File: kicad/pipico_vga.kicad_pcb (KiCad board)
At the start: 2 copper layers, 47 parts, among them J1 Conn_01x15, J2 DB15_Male_HighDensity_Mountin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, U1 Pico, U2 74LVC162244ADGVJ

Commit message: progress on pcb rev2
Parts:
- moved TP4 99.9 mm to (160.4, 106.9)
- moved R22 94.0 mm to (115.9, 94.5), turned to 180 degrees
- moved R17 94.0 mm to (116.8, 97.1), turned to 270 degrees
- moved R21 92.6 mm to (114.1, 92.8), turned to 180 degrees
- moved R16 91.6 mm to (115.0, 97.1), turned to 270 degrees
- moved R20 89.3 mm to (112.4, 94.5), turned to 180 degrees
- moved R15 89.2 mm to (113.2, 97.1), turned to 270 degrees
- moved TP6 89.1 mm to (156.2, 115.7), turned to 180 degrees
- moved U1 88.5 mm to (114.2, 109.1)
- moved R19 88.1 mm to (110.6, 92.8), turned to 180 degrees
- moved R14 86.8 mm to (111.5, 97.1), turned to 270 degrees
- moved R18 84.7 mm to (108.9, 94.5), turned to 180 degrees
- moved R13 84.5 mm to (109.8, 97.1), turned to 270 degrees
- moved C1 84.3 mm to (111.8, 102.2), turned to 90 degrees
- moved C4 83.4 mm to (113.8, 102.2), turned to 90 degrees
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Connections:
- net Net-(R15-Pad2) renamed /r2
- J1 pad 11: Net-(J1-Pad11) -> +3V3
- J1 pad 5: +3V3 -> Net-(J1-Pad5)
- R13 pad 2: Net-(R13-Pad2) -> /r0
- R14 pad 2: Net-(R14-Pad2) -> /r1
- R16 pad 2: Net-(R16-Pad2) -> /r3
- R17 pad 2: Net-(R17-Pad2) -> /r4
- R2 pad 2: Net-(R2-Pad2) -> /g0
- R24 pad 2: Net-(R24-Pad2) -> /b0
- R25 pad 2: Net-(R25-Pad2) -> /b1
- R26 pad 2: Net-(R26-Pad2) -> /b2
- R27 pad 2: Net-(R27-Pad2) -> /b3
- R28 pad 2: Net-(R28-Pad2) -> /b4
- R3 pad 2: Net-(R3-Pad2) -> /g1
- R4 pad 2: Net-(R4-Pad2) -> /g2
- R5 pad 2: Net-(R5-Pad2) -> /g3
- R6 pad 2: Net-(R6-Pad2) -> /g4
- U1 pad 21: /vga_data -> /hsync
- U1 pad 22: /vga_clk -> /vsync
- U1 pad 24: /vsync -> /vga_data
- U1 pad 25: /hsync -> /vga_clk
- U1 pad 26: Net-(J1-Pad15) -> Net-(J1-Pad1)
- U1 pad 27: Net-(J1-Pad14) -> Net-(J1-Pad2)
- U1 pad 29: Net-(J1-Pad12) -> Net-(J1-Pad4)
- U1 pad 30: Net-(J1-Pad11) -> Net-(J1-Pad5)
- U1 pad 31: Net-(J1-Pad10) -> Net-(J1-Pad6)
- U1 pad 32: Net-(J1-Pad9) -> Net-(J1-Pad7)
- U1 pad 34: Net-(J1-Pad7) -> Net-(J1-Pad9)
- U1 pad 35: Net-(J1-Pad6) -> Net-(J1-Pad10)
- U1 pad 37: Net-(J1-Pad4) -> Net-(J1-Pad12)
- U1 pad 39: Net-(J1-Pad2) -> Net-(J1-Pad14)
- U1 pad 40: Net-(J1-Pad1) -> Net-(J1-Pad15)
- U2 pad 11: /gpio6 -> /gpio8
- U2 pad 13: /gpio8 -> /gpio6
- U2 pad 14: /gpio9 -> /gpio5
- U2 pad 16: /gpio10 -> /gpio4
- U2 pad 17: /gpio11 -> /gpio3
- U2 pad 19: /gpio12 -> /gpio2
- U2 pad 2: /gpio0 -> /gpio14
- U2 pad 20: /gpio13 -> /gpio1
- U2 pad 22: /gpio14 -> /gpio0
- U2 pad 27: Net-(R17-Pad2) -> /r0
- U2 pad 29: Net-(R16-Pad2) -> /r1
- U2 pad 3: /gpio1 -> /gpio13
- U2 pad 32: Net-(R14-Pad2) -> /r3
- U2 pad 33: Net-(R13-Pad2) -> /r4
- U2 pad 35: Net-(R6-Pad2) -> /b0
- U2 pad 36: Net-(R5-Pad2) -> /b1
- U2 pad 37: Net-(R4-Pad2) -> /b2
- U2 pad 38: Net-(R3-Pad2) -> /b3
- U2 pad 40: Net-(R2-Pad2) -> /b4
- U2 pad 41: Net-(R28-Pad2) -> /g0
- U2 pad 43: Net-(R27-Pad2) -> /g1
- U2 pad 44: Net-(R26-Pad2) -> /g2
- U2 pad 46: Net-(R25-Pad2) -> /g3
- U2 pad 47: Net-(R24-Pad2) -> /g4
- U2 pad 5: /gpio3 -> /gpio12
- U2 pad 6: (no net) -> /gpio11
- U2 pad 8: /gpio4 -> /gpio10
- U2 pad 9: /gpio5 -> /gpio9
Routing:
- net /vga_data: track 95.4 -> 0.00 mm
- net /hsync: track 79.4 -> 0.00 mm
- net /vsync: track 76.6 -> 0.00 mm
- net /vga_clk: track 75.5 -> 0.00 mm
- net +3V3: track 125.0 -> 72.8 mm, vias 5 -> 4
- net GND: track 71.3 -> 26.1 mm, vias 9 -> 0
- net /b0: track 0.00 -> 24.9 mm, vias 0 -> 2
- net /b1: track 0.00 -> 22.8 mm, vias 0 -> 2
- net /b2: track 0.00 -> 21.8 mm, vias 0 -> 2
- net /b3: track 0.00 -> 19.7 mm, vias 0 -> 2
- net /b4: track 0.00 -> 18.2 mm, vias 0 -> 2
- net /red: track 38.1 -> 55.8 mm, vias 0 -> 2
- net /gpio2: track 0.00 -> 14.0 mm
- net Net-(R17-Pad2): track 12.5 -> 0.00 mm
- net Net-(R16-Pad2): track 11.9 -> 0.00 mm
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- removed copper zone on B.Cu, net GND
- removed copper zone on F.Cu, net GND
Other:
- net class Default: clearance 0.2 -> 0.3; via_dia 1.5 -> 0.8
- net class tiny added: clearance 0.2, trace_width 0.3, via_dia 0.8, via_drill 0.4
- rule trace_clearance: 0.2 -> 0.3
- board text removed: "PICO VGA V2 Anton Lööf"

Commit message: Add v2 PCB
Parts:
- BLUE: renamed from TP3; footprint TestPoint:TestPoint_Pad_D1.5mm -> TestPoint:TestPoint_THTPad_D2.0mm_Drill1.0mm; moved to B.Cu
- C1, C2, C3, C4, J1, J2, U1: moved to F.Cu
- GND: renamed from TP6; footprint TestPoint:TestPoint_Pad_D1.5mm -> TestPoint:TestPoint_THTPad_D2.0mm_Drill1.0mm; moved to B.Cu
- GND: renamed from TP5; footprint TestPoint:TestPoint_Pad_D1.5mm -> TestPoint:TestPoint_THTPad_D2.0mm_Drill1.0mm; moved to B.Cu
- GND: renamed from TP4; footprint TestPoint:TestPoint_Pad_D1.5mm -> TestPoint:TestPoint_THTPad_D2.0mm_Drill1.0mm; moved to B.Cu
- GREEN: renamed from TP2; footprint TestPoint:TestPoint_Pad_D1.5mm -> TestPoint:TestPoint_THTPad_D2.0mm_Drill1.0mm; moved to B.Cu
- R1, R10, R11, R12, R13, R14, R15, R16, R17, R18, R19, R2, R20, R21, R22, R23, R24, R25, R26, R27, R28, R29, R3, R30, R31, R32, R33, R4, R5, R6, R7, R8, R9, U2: moved to B.Cu
- RED: renamed from TP1; footprint TestPoint:TestPoint_Pad_D1.5mm -> TestPoint:TestPoint_THTPad_D2.0mm_Drill1.0mm; moved to B.Cu
- moved J2 67.4 mm to (137.7, 79.4)
- moved RED 57.9 mm to (131.8, 85.0)
- moved BLUE 53.9 mm to (131.8, 93.0), turned to 270 degrees
- moved GREEN 52.4 mm to (131.8, 89.0)
- moved R30 51.2 mm to (146.9, 89.0)
- moved R32 51.2 mm to (143.4, 89.0)
- moved R29 48.5 mm to (148.6, 90.8)
- moved R31 48.5 mm to (145.1, 90.8)
- moved R33 48.5 mm to (141.6, 90.8)
- moved GND 46.5 mm to (126.8, 89.0)
- moved R19 45.6 mm to (142.6, 125.2)
- moved R21 45.6 mm to (146.1, 125.2)
- moved R23 44.7 mm to (149.5, 93.4), turned to 270 degrees
- moved R24 44.7 mm to (147.8, 93.4), turned to 270 degrees
- moved R25 44.7 mm to (146.0, 93.4), turned to 270 degrees
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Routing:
- net /vga_clk: track 0.00 -> 50.2 mm
- net GND: track 26.1 -> 74.2 mm, vias 0 -> 3
- net /vsync: track 0.00 -> 32.4 mm
- net /vga_data: track 0.00 -> 29.3 mm
- net /blue: track 13.4 -> 38.6 mm
- net +3V3: track 72.8 -> 49.2 mm
- net /hsync: track 0.00 -> 22.4 mm
- net /green: track 22.5 -> 35.2 mm
- net /red: track 55.8 -> 64.7 mm, vias 2 -> 1
- added copper zone on B.Cu, net GND
- added copper zone on F.Cu, net GND
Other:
- board outline added: 37 x 67 mm
- board text added: "Anton Lööf 2021 REV2"
- board text added: "Raspberry pi Pico VGA"
- board text added: "VBUS VSYS GND 3V3EN 3V3 AREF GP28 GND GP27 GP26 RUN GP22 GND GP21 GP20"

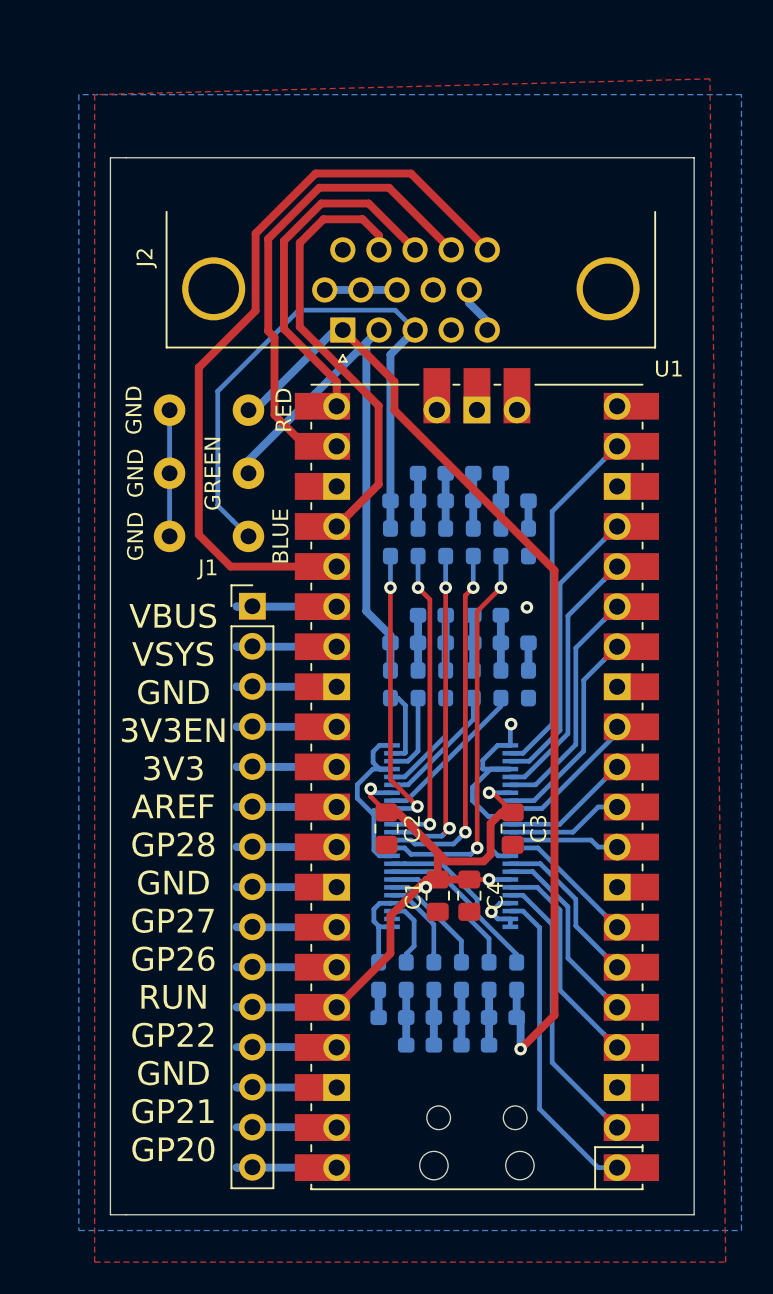
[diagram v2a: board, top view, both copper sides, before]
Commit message: Add mounting hole
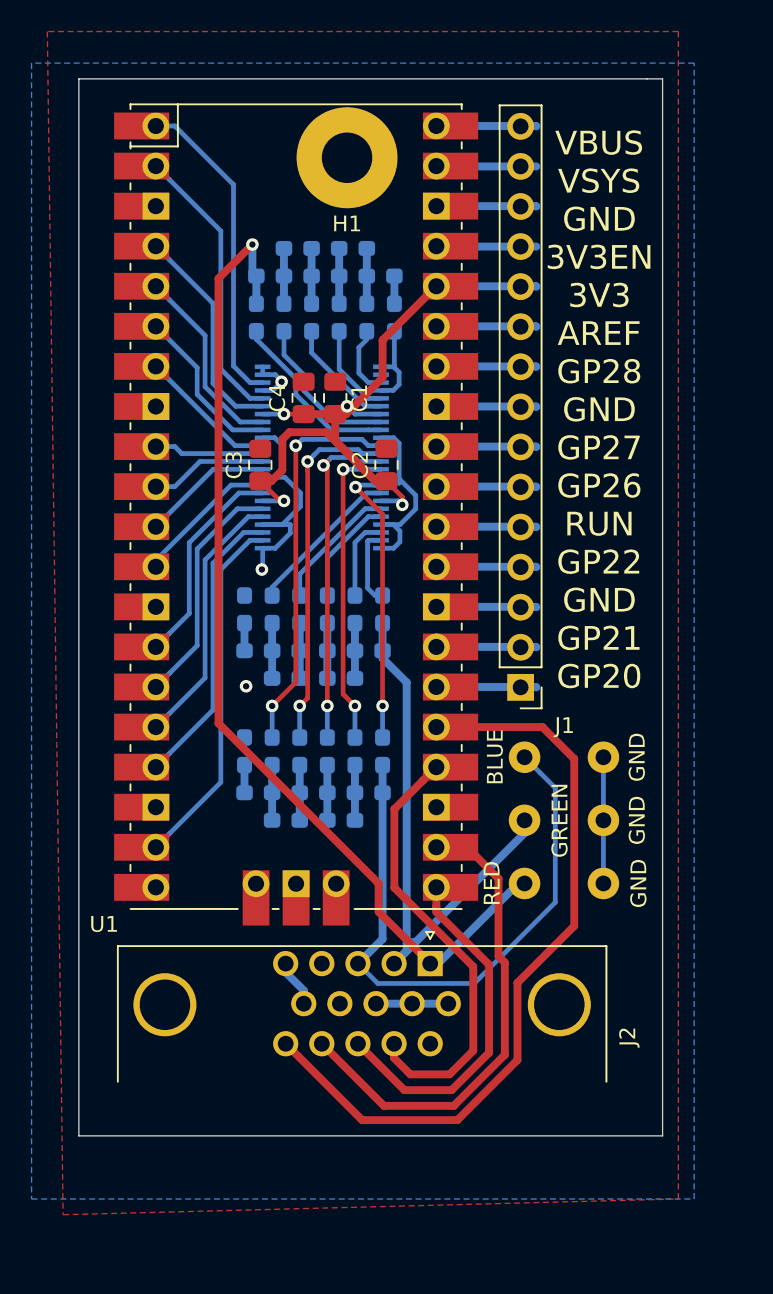
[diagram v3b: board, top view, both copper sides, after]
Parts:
- added H1: MountingHole_Pad, MountingHole:MountingHole_3.2mm_M3_Pad, F.Cu at (138.0, 69.0)
- moved R21 51.7 mm to (134.9, 74.8), turned to 0 degrees
- moved R19 50.7 mm to (138.4, 74.8), turned to 0 degrees
- moved R22 49.3 mm to (133.1, 76.5), turned to 0 degrees
- moved R20 47.6 mm to (136.6, 76.5), turned to 0 degrees
- moved R18 47.0 mm to (140.1, 76.5), turned to 0 degrees
- moved R17 44.9 mm to (132.2, 79.1), turned to 270 degrees
- moved R16 43.7 mm to (134.0, 79.1), turned to 270 degrees
- moved R15 42.8 mm to (135.8, 79.1), turned to 270 degrees
- moved R14 42.2 mm to (137.5, 79.1), turned to 270 degrees
- moved R13 41.8 mm to (139.2, 79.1), turned to 270 degrees
- moved R12 41.8 mm to (141.0, 79.1), turned to 270 degrees
- moved J2 41.7 mm to (143.3, 120.6), turned to 0 degrees
- moved GND 40.7 mm to (154.2, 115.0), turned to 0 degrees
- moved GND 35.2 mm to (154.2, 111.0), turned to 0 degrees
- moved RED 34.7 mm to (149.2, 115.0), turned to 0 degrees
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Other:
- outline, holes or cut-outs redrawn

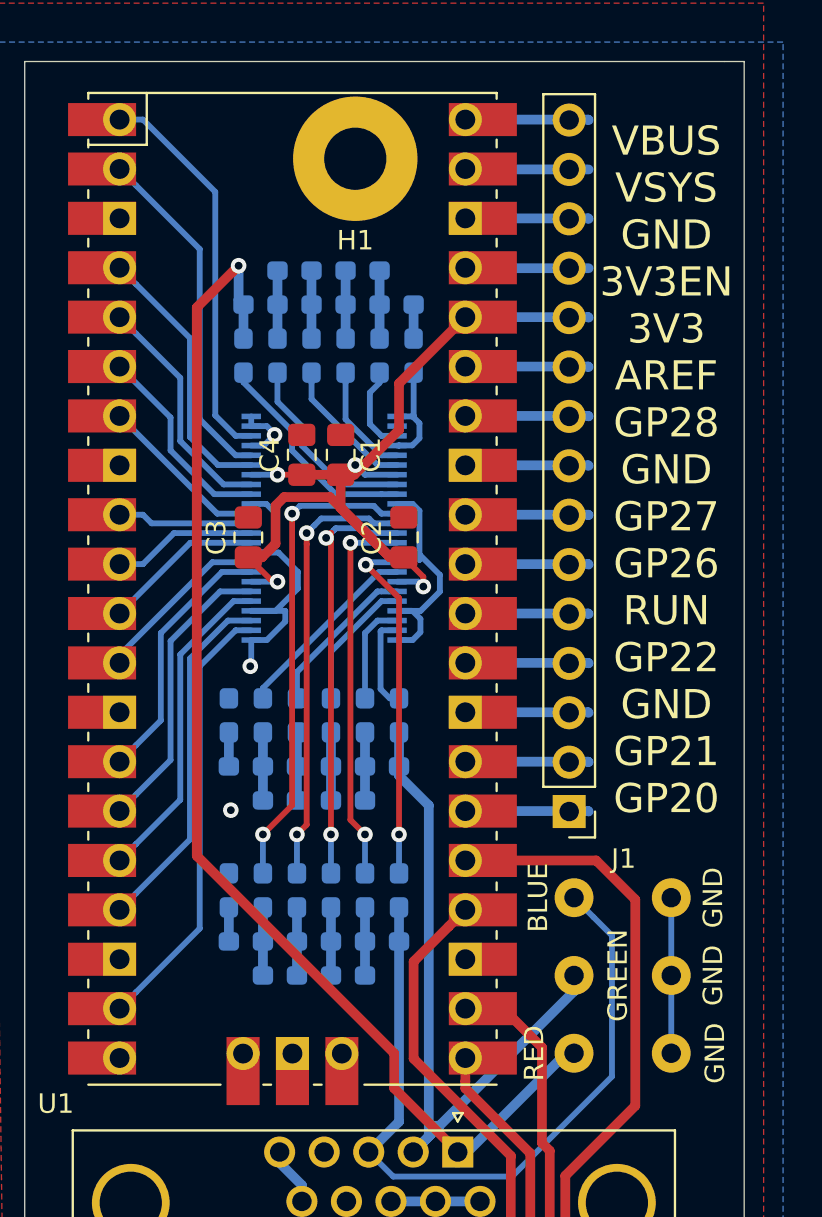
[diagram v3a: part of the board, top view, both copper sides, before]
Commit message: Rev3 pcb now correct footprint of buffer
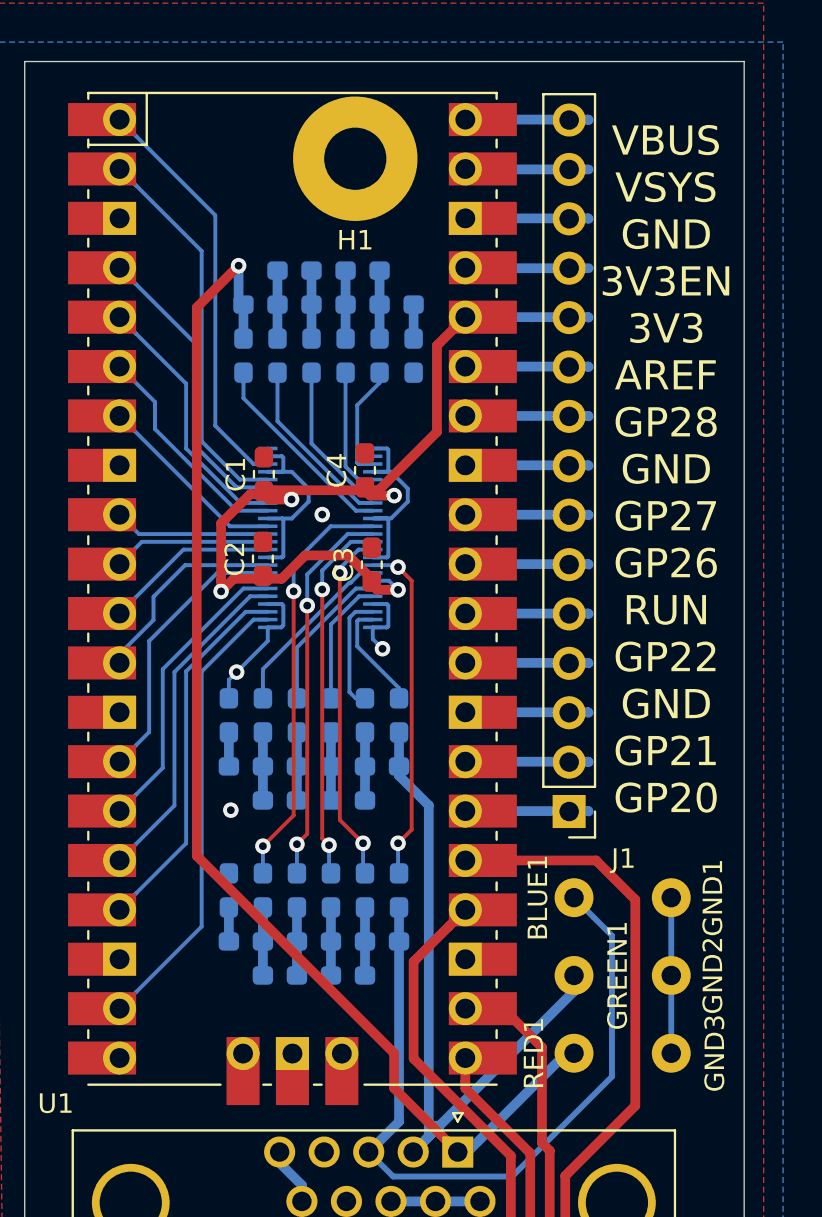
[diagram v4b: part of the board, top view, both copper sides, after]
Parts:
- C1, C2, C3, C4: footprint Capacitor_SMD:C_0805_2012Metric_Pad1.15x1.40mm_HandSolder -> Capacitor_SMD:C_0603_1608Metric_Pad1.05x0.95mm_HandSolder
- U2: footprint Package_SO:TSSOP-48_6.1x12.5mm_P0.5mm -> good_things:SOIC-48
- moved C2 7.33 mm to (133.2, 89.6)
- moved C3 6.50 mm to (138.8, 89.9)
- moved C1 4.07 mm to (133.3, 85.2)
- moved C4 3.35 mm to (138.5, 85.0)
- moved U2 0.54 mm to (136.2, 88.5), turned to 90 degrees
- renumbered BLUE to BLUE1, GND to GND1, GND to GND2, GND to GND3, GREEN to GREEN1, RED to RED1
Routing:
- net GND: track 74.2 -> 67.5 mm, vias 3 -> 4
- net /b0: track 24.9 -> 21.5 mm
- net /b1: track 22.8 -> 19.8 mm
- net /b2: track 21.8 -> 19.0 mm
- net /gpio1: track 18.0 -> 20.0 mm
- net /gpio9: track 9.15 -> 10.7 mm
- net /gpio2: track 14.0 -> 15.4 mm
- net /r0: track 4.51 -> 5.94 mm
- net /b3: track 19.7 -> 18.3 mm
- net /gpio3: track 12.2 -> 13.5 mm
- net /gpio5: track 8.85 -> 9.97 mm
- net /gpio6: track 6.95 -> 8.03 mm
- net /gpio0: track 20.2 -> 21.3 mm
- net /gpio4: track 10.5 -> 11.5 mm
- net /r4: track 11.4 -> 10.4 mm
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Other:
- net class Default: clearance 0.3 -> 0.2
- net class tiny removed
- rule trace_clearance: 0.3 -> 0.2
- board text added: "Anton Lööf 2021 REV3"
- board text removed: "Anton Lööf 2021 REV2"
